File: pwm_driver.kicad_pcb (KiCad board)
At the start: 2 copper layers, 56.6 x 57.7 mm, 41 parts, among them J1 V_{In}, J2 GND_{In}, J3 SolderPad, J4 SolderPad, Q1 BC817, Q2 BC807, Q3 TSM900N06CW_RPG, U1 TLV2372, U2 LM393

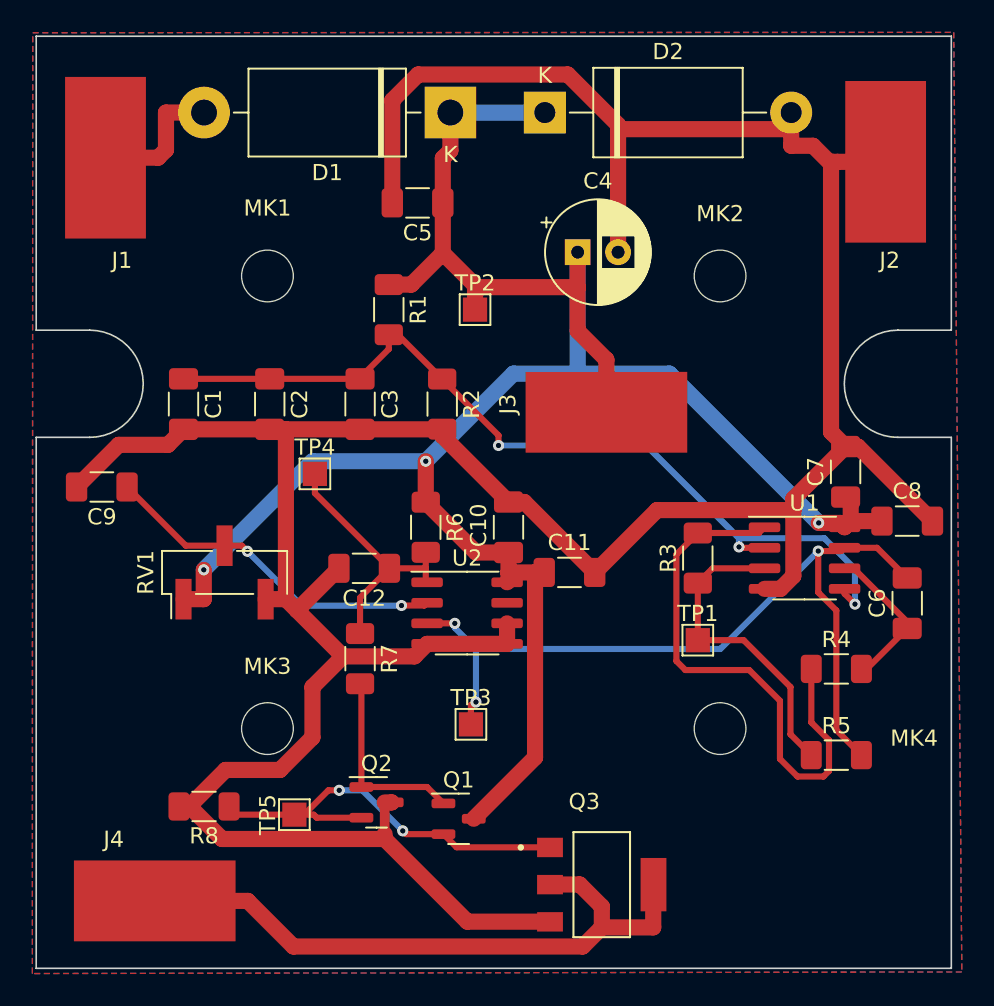
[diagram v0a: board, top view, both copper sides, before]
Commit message: trace width modified for higher currents
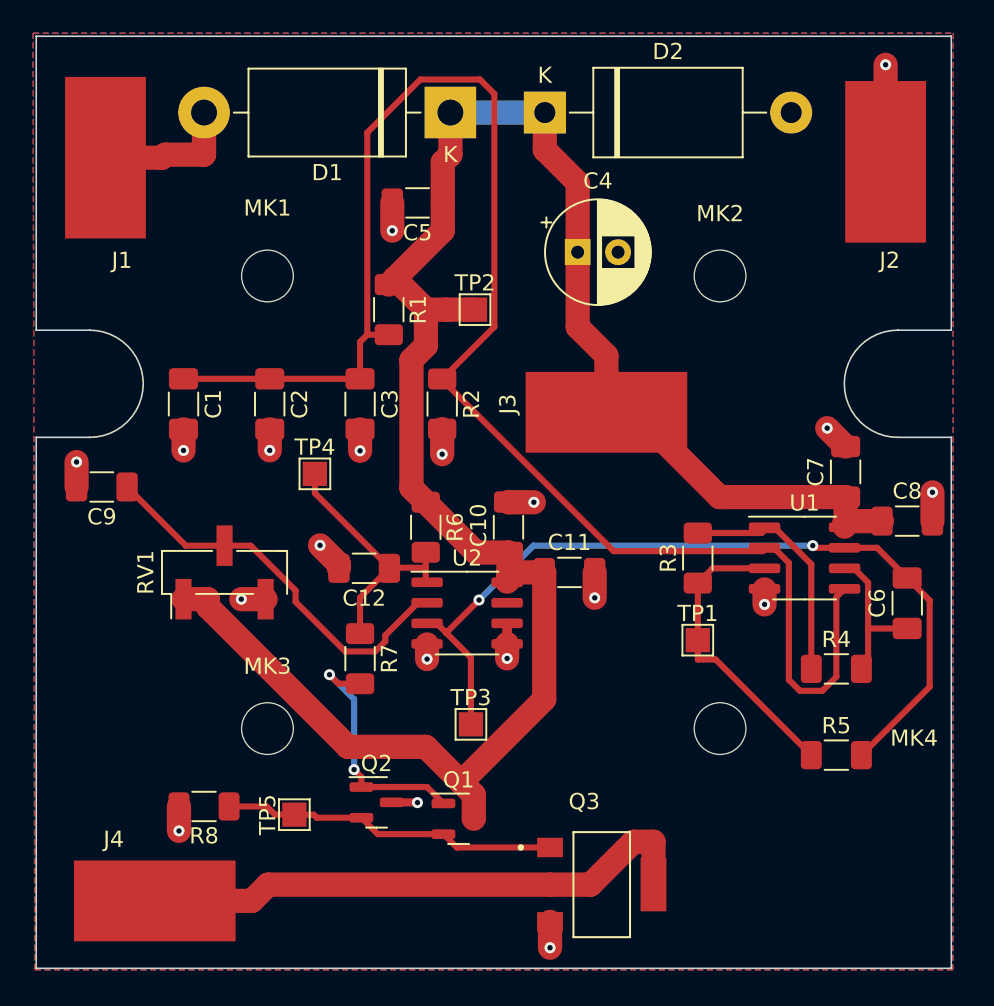
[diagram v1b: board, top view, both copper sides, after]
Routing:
- net GND: track 213.2 -> 33.5 mm, vias 0 -> 19
- net /U_{cc}/2: track 55.1 -> 99.1 mm, vias 3 -> 0
- net /U_{ST}: track 34.2 -> 14.6 mm
- net /FET_Drain: track 40.1 -> 35.0 mm
- net /U_{FET_driver}: track 25.9 -> 20.9 mm, vias 2 -> 0
- net VCC: track 133.3 -> 128.8 mm, vias 3 -> 0
- net Net-(Q1-Pad1): track 11.9 -> 15.4 mm, vias 0 -> 2
- net /U_{Pot}: track 21.7 -> 24.6 mm, vias 2 -> 0
- net Net-(R3-Pad1): track 19.7 -> 18.7 mm
- net /U_{Triangle}: track 52.5 -> 52.6 mm, vias 3 -> 2

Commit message: minor layout modifications
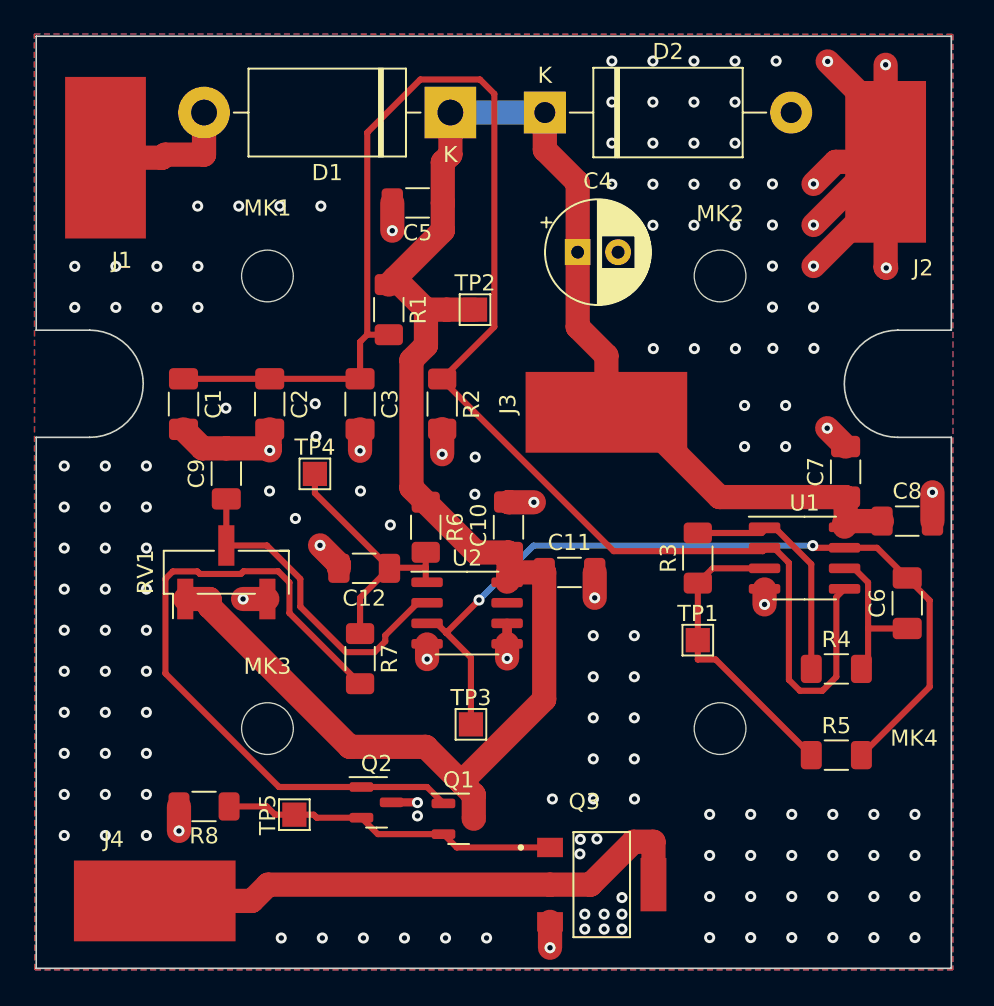
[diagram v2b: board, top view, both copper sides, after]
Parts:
- moved C9 7.74 mm to (85.2, 108.9), turned to 90 degrees
- moved RV1 0.11 mm to (85.2, 115.0)
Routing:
- net GND: track 33.5 -> 70.2 mm, vias 19 -> 159
- net Net-(Q1-Pad1): track 15.4 -> 42.7 mm, vias 2 -> 0
- net /U_{Pot}: track 24.6 -> 20.5 mm

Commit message: minor layout modifications
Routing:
- net GND: track 70.2 -> 172.7 mm, vias 159 -> 162
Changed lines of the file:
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@@
   (segment (start 114.317 119.177) (end 114.317 120.3718) (width 0.381) (layer "F.Cu") (net 5))
   (segment (start 121.338 126.289) (end 115.4208 120.3718) (width 0.381) (layer "F.Cu") (net 5))
+  (segment (start 125.975 96.15) (end 125.975 90.075) (width 1.5) (layer "F.Cu") (net 6))
   (segment (start 97.57 120.3488) (end 97.57 119.4401) (width 1.5) (layer "F.Cu") (net 6))
+  (segment (start 122.35 83.375) (end 122.35 86.45) (width 1.5) (layer "F.Cu") (net 6))
+  (segment (start 122.35 84.282) (end 120.094 86.538) (width 1.5) (layer "F.Cu") (net 6))
+  (segment (start 122.425 86.525) (end 122.425 92.545) (width 1.5) (layer "F.Cu") (net 6))
+  (segment (start 124.125 95) (end 124.125 91.397) (width 1.5) (layer "F.Cu") (net 6))
   (segment (start 122.3218 106.0613) (end 123.461 107.2005) (width 1.5) (layer "F.Cu") (net 6))
+  (segment (start 125.975 96.15) (end 121.59 96.15) (width 1.5) (layer "F.Cu") (net 6))
   (segment (start 98.504 107.6744) (end 98.504 106.122) (width 1.5) (layer "F.Cu") (net 6))
   (segment (start 85.15 107.3125) (end 83.68 107.3125) (width 1.5) (layer "F.Cu") (net 6))
   (segment (start 87.69 116.63) (end 86.1857 116.63) (width 1.5) (layer "F.Cu") (net 6))
+  (segment (start 122.35 86.45) (end 122.425 86.525) (width 1.5) (layer "F.Cu") (net 6))
   (segment (start 125.384 89.586) (end 121.475 93.495) (width 1.5) (layer "F.Cu") (net 6))
   (segment (start 125.936 89.586) (end 125.936 86.961) (width 1.5) (layer "F.Cu") (net 6))
+  (segment (start 123.142 89.586) (end 120.094 86.538) (width 1.5) (layer "F.Cu") (net 6))
   (segment (start 125.936 91.574) (end 121.475 96.035) (width 1.5) (layer "F.Cu") (net 6))
   (segment (start 102.52 120.3076) (end 102.52 119.405) (width 1.5) (layer "F.Cu") (net 6))
   (segment (start 125.936 89.586) (end 125.936 91.574) (width 1.5) (layer "F.Cu") (net 6))
   (segment (start 95.4175 92.126) (end 95.4175 93.8461) (width 1.5) (layer "F.Cu") (net 6))
+  (segment (start 125.975 96.15) (end 125.975 92.419) (width 1.5) (layer "F.Cu") (net 6))
   (segment (start 93.424 107.4624) (end 93.424 106.1345) (width 1.5) (layer "F.Cu") (net 6))
+  (segment (start 125.975 96.15) (end 125.275 96.15) (width 1.5) (layer "F.Cu") (net 6))
   (segment (start 125.936 89.586) (end 122.844 89.586) (width 1.5) (layer "F.Cu") (net 6))
   (segment (start 102.52 118.135) (end 102.52 119.405) (width 0.601) (layer "F.Cu") (net 6))
+  (segment (start 125.975 96.15) (end 125.975 95.455) (width 1.5) (layer "F.Cu") (net 6))
   (segment (start 118.446 116.0371) (end 118.446 116.002) (width 0.601) (layer "F.Cu") (net 6))
   (segment (start 87.836 107.3125) (end 85.15 107.3125) (width 1.5) (layer "F.Cu") (net 6))
   (segment (start 118.446 116.9653) (end 118.446 116.0371) (width 1.5) (layer "F.Cu") (net 6))
   (segment (start 104.1762 110.6464) (end 102.6234 110.6464) (width 1.5) (layer "F.Cu") (net 6))
+  (segment (start 125.975 91.925) (end 122.425 88.375) (width 1.5) (layer "F.Cu") (net 6))
   (segment (start 97.57 119.4401) (end 97.57 119.405) (width 0.601) (layer "F.Cu") (net 6))
   (segment (start 125.936 89.586) (end 125.936 83.5817) (width 1.5) (layer "F.Cu") (net 6))
+  (segment (start 122.425 92.545) (end 121.475 93.495) (width 1.5) (layer "F.Cu") (net 6))
+  (segment (start 121.59 96.15) (end 121.475 96.035) (width 1.5) (layer "F.Cu") (net 6))
   (segment (start 102.6234 110.6464) (end 102.6065 110.6295) (width 1.5) (layer "F.Cu") (net 6))
   (segment (start 87.836 107.4387) (end 87.836 107.3125) (width 1.5) (layer "F.Cu") (net 6))
+  (segment (start 122.412 86.538) (end 122.425 86.525) (width 1.5) (layer "F.Cu") (net 6))
+  (segment (start 122.425 95.085) (end 121.475 96.035) (width 1.5) (layer "F.Cu") (net 6))
   (segment (start 122.844 89.586) (end 121.475 90.955) (width 1.5) (layer "F.Cu") (net 6))
+  (segment (start 125.975 90.075) (end 122.425 86.525) (width 1.5) (layer "F.Cu") (net 6))
   (segment (start 96.96 129.21) (end 96.975 129.225) (width 0.508) (layer "F.Cu") (net 6))
+  (segment (start 125.936 83.5817) (end 125.3683 83.5817) (width 1.5) (layer "F.Cu") (net 6))
+  (segment (start 122.425 90.005) (end 121.475 90.955) (width 1.5) (layer "F.Cu") (net 6))
+  (segment (start 122.425 88.375) (end 122.425 95.085) (width 1.5) (layer "F.Cu") (net 6))
+  (segment (start 123.0503 83.5817) (end 120.094 86.538) (width 1.5) (layer "F.Cu") (net 6))
+  (segment (start 122.35 83.375) (end 122.35 84.282) (width 1.5) (layer "F.Cu") (net 6))
   (segment (start 128.8335 110.0312) (end 128.8335 111.811) (width 1.5) (layer "F.Cu") (net 6))
+  (segment (start 125.936 89.586) (end 123.142 89.586) (width 1.5) (layer "F.Cu") (net 6))
   (segment (start 125.936 89.586) (end 125.384 89.586) (width 1.5) (layer "F.Cu") (net 6))
   (segment (start 92.1155 114.732) (end 92.1155 114.4795) (width 1.5) (layer "F.Cu") (net 6))
   (segment (start 107.9405 116.5586) (end 107.9405 114.986) (width 1.5) (layer "F.Cu") (net 6))
+  (segment (start 125.936 89.586) (end 125.486 89.586) (width 1.5) (layer "F.Cu") (net 6))
   (segment (start 92.1155 114.4795) (end 90.9476 113.3116) (width 1.5) (layer "F.Cu") (net 6))
+  (segment (start 125.275 96.15) (end 124.125 95) (width 1.5) (layer "F.Cu") (net 6))
   (segment (start 105.175 136.6) (end 105.175 138.2043) (width 1.5) (layer "F.Cu") (net 6))
   (segment (start 125.936 86.961) (end 122.35 83.375) (width 1.5) (layer "F.Cu") (net 6))
+  (segment (start 124.13 96.15) (end 121.475 93.495) (width 1.5) (layer "F.Cu") (net 6))
   (segment (start 87.836 107.3125) (end 87.836 106.1345) (width 1.5) (layer "F.Cu") (net 6))
-  (segment (start 125.936 96.111) (end 125.975 96.15) (width 1.5) (layer "F.Cu") (net 6))
-  (segment (start 125.936 89.586) (end 125.936 96.111) (width 1.5) (layer "F.Cu") (net 6))
+  (segment (start 125.975 96.15) (end 125.975 91.925) (width 1.5) (layer "F.Cu") (net 6))
+  (segment (start 122.425 86.525) (end 122.425 88.375) (width 1.5) (layer "F.Cu") (net 6))
+  (segment (start 125.936 83.5817) (end 123.0503 83.5817) (width 1.5) (layer "F.Cu") (net 6))
+  (segment (start 125.975 96.15) (end 124.13 96.15) (width 1.5) (layer "F.Cu") (net 6))
+  (segment (start 124.125 91.397) (end 125.936 89.586) (width 1.5) (layer "F.Cu") (net 6))
   (segment (start 83.68 107.3125) (end 82.502 106.1345) (width 1.5) (layer "F.Cu") (net 6))
+  (segment (start 125.975 92.419) (end 123.142 89.586) (width 1.5) (layer "F.Cu") (net 6))
+  (segment (start 125.3683 83.5817) (end 122.425 86.525) (width 1.5) (layer "F.Cu") (net 6))
+  (segment (start 120.094 86.538) (end 122.412 86.538) (width 1.5) (layer "F.Cu") (net 6))
+  (segment (start 122.425 86.525) (end 122.425 90.005) (width 1.5) (layer "F.Cu") (net 6))
   (segment (start 95.3815 129.21) (end 96.96 129.21) (width 0.508) (layer "F.Cu") (net 6))
+  (segment (start 125.975 95.455) (end 121.475 90.955) (width 1.5) (layer "F.Cu") (net 6))
   (segment (start 82.222 130.9774) (end 82.222 129.464) (width 1.5) (layer "F.Cu") (net 6))
+  (segment (start 125.486 89.586) (end 122.425 86.525) (width 1.5) (layer "F.Cu") (net 6))
   (via (at 122.3218 106.0613) (size 0.6858) (drill 0.3302) (layers "F.Cu" "B.Cu") (net 6))
   (via (at 109.625 137.05) (size 0.6858) (drill 0.3302) (layers "F.Cu" "B.Cu") (free) (net 6))
@@
   (via (at 75.775 96.05) (size 0.6858) (drill 0.3302) (layers "F.Cu" "B.Cu") (free) (net 6))
   (via (at 118.935 90.955) (size 0.6858) (drill 0.3302) (layers "F.Cu" "B.Cu") (free) (net 6))
+  (via (at 82.525 110.95) (size 0.6858) (drill 0.3302) (layers "F.Cu" "B.Cu") (free) (net 6))
   (via (at 107.86 129) (size 0.6858) (drill 0.3302) (layers "F.Cu" "B.Cu") (free) (net 6))
   (via (at 80.205 116.02) (size 0.6858) (drill 0.3302) (layers "F.Cu" "B.Cu") (free) (net 6))
@@
   (via (at 127.75 137.575) (size 0.6858) (drill 0.3302) (layers "F.Cu" "B.Cu") (free) (net 6))
   (via (at 111.565 101.14) (size 0.6858) (drill 0.3302) (layers "F.Cu" "B.Cu") (free) (net 6))
+  (via (at 82.525 108.375) (size 0.6858) (drill 0.3302) (layers "F.Cu" "B.Cu") (free) (net 6))
   (via (at 116.62 90.97) (size 0.6858) (drill 0.3302) (layers "F.Cu" "B.Cu") (free) (net 6))
   (via (at 111.54 83.35) (size 0.6858) (drill 0.3302) (layers "F.Cu" "B.Cu") (free) (net 6))
@@
   (via (at 82.222 130.9774) (size 0.6858) (drill 0.3302) (layers "F.Cu" "B.Cu") (net 6))
   (via (at 75.775 98.59) (size 0.6858) (drill 0.3302) (layers "F.Cu" "B.Cu") (free) (net 6))
+  (via (at 122.425 86.525) (size 0.6858) (drill 0.3302) (layers "F.Cu" "B.Cu") (free) (net 6))
   (via (at 86.1857 116.63) (size 0.6858) (drill 0.3302) (layers "F.Cu" "B.Cu") (net 6))
   (via (at 117.21 107.2) (size 0.6858) (drill 0.3302) (layers "F.Cu" "B.Cu") (free) (net 6))
